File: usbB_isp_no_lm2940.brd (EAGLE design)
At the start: 56 x 20 mm, 9 parts, among them IC2 TINY13-20PU, X1 PN61729-S

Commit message: minor adjustments (tm)
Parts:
- moved C3 0.23 mm to (44.4, 5.65)
- moved IC2 0.23 mm to (37.2, 6.20)
- moved LED1 0.23 mm to (14.6, 9.03)
- moved R1 0.23 mm to (38.7, 13.5)
- moved R2 0.23 mm to (26.2, 12.0)
- moved R3 0.23 mm to (26.5, 5.84)
- moved SV2 0.23 mm to (49.3, 9.03)
- moved X1 0.09 mm to (2.47, 8.94)
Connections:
- net GND: now also X1.2
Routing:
- net GND: track 17.1 -> 25.0 mm

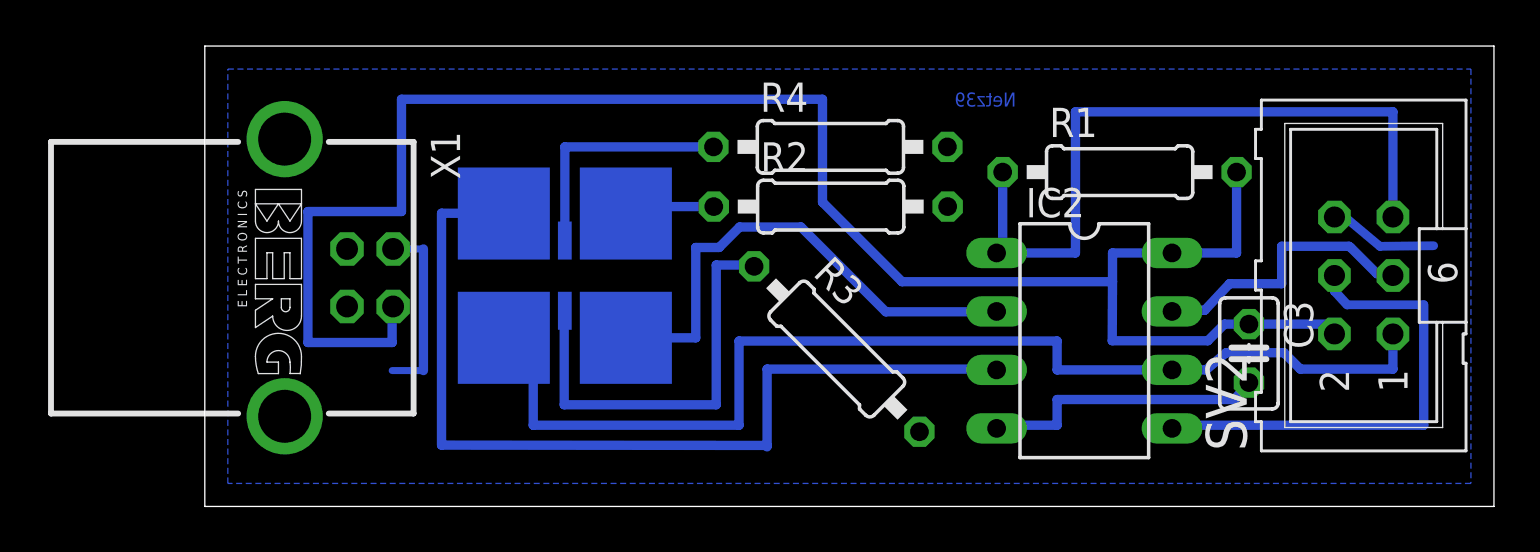
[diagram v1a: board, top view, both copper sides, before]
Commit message: wrong usb-pin *again and again and again and again …
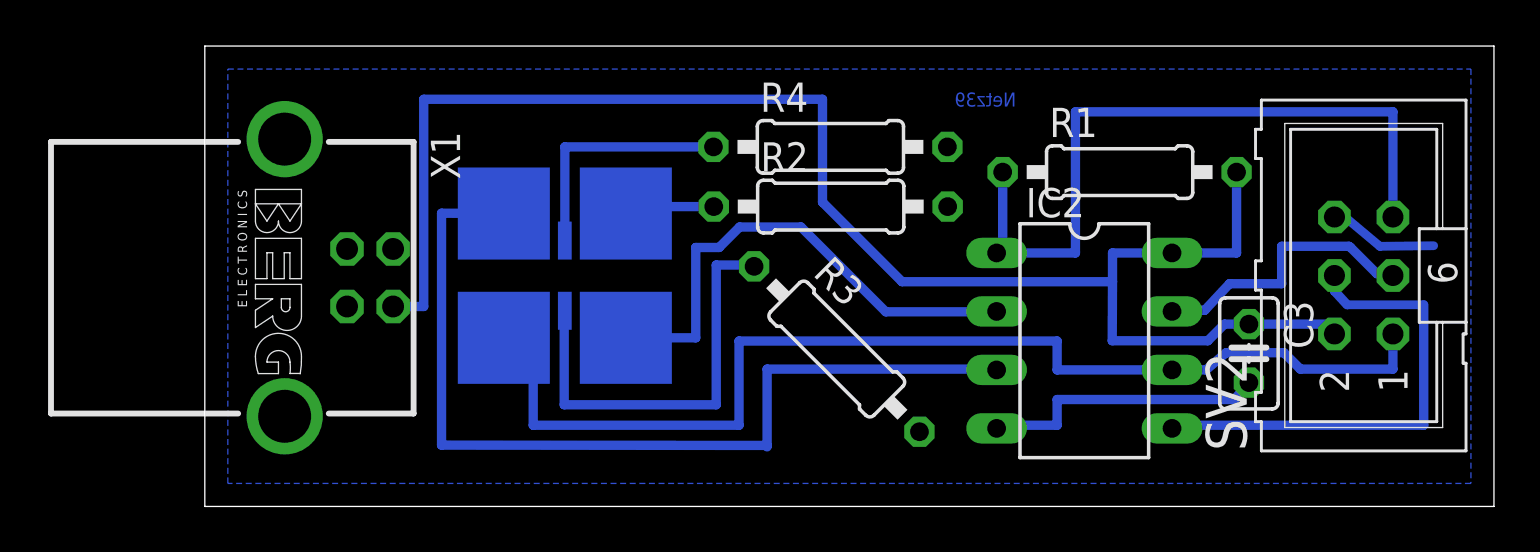
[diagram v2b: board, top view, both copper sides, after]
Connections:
- net GND: now also X1.4; no longer X1.2
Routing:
- net VCC: track 79.8 -> 69.3 mm
- net GND: track 25.0 -> 17.1 mm
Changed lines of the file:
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@@
 <setting verticaltext="up"/>
 </settings>
-<grid distance="39.3700787" unitdist="mil" unit="mil" style="dots" multiple="1" display="yes" altdistance="0.0254" altunitdist="mm" altunit="mm"/>
+<grid distance="1" unitdist="mil" unit="mil" style="dots" multiple="1" display="yes" altdistance="0.0254" altunitdist="mm" altunit="mm"/>
 <layers>
 <layer number="1" name="Top" color="4" fill="1" visible="yes" active="yes"/>
@@
 <wire x1="36.0238" y1="3.6454" x2="43.7228" y2="3.6454" width="0.4064" layer="16"/>
 <wire x1="43.7228" y1="3.6454" x2="44.356" y2="4.3802" width="0.4064" layer="16"/>
-<contactref element="X1" pad="2"/>
-<wire x1="7.1789" y1="10.186" x2="8.4963" y2="10.186" width="0.3048" layer="16"/>
-<wire x1="8.4963" y1="10.186" x2="8.4963" y2="4.9022" width="0.4064" layer="16"/>
-<wire x1="8.4963" y1="4.9022" x2="7.1374" y2="4.9022" width="0.3048" layer="16"/>
 <polygon width="0.4064" layer="16" isolate="0.5842" thermals="no">
 <vertex x="0" y="0"/>
@@
 <vertex x="54" y="0"/>
 </polygon>
+<contactref element="X1" pad="4"/>
 </signal>
 <signal name="VCC">
@@
 <wire x1="44.356" y1="6.9202" x2="48.0716" y2="6.9202" width="0.4064" layer="16"/>
 <wire x1="48.0716" y1="6.9202" x2="48.0716" y2="6.493" width="0.4064" layer="16"/>
-<wire x1="7.1789" y1="7.686" x2="7.1374" y2="7.686" width="0.4064" layer="16"/>
-<wire x1="7.1374" y1="7.686" x2="7.1374" y2="6.1214" width="0.4064" layer="16"/>
-<wire x1="7.1374" y1="6.1214" x2="3.4798" y2="6.1214" width="0.4064" layer="16"/>
-<wire x1="3.4798" y1="6.1214" x2="3.4798" y2="11.811" width="0.4064" layer="16"/>
-<wire x1="3.4798" y1="11.811" x2="7.5438" y2="11.811" width="0.4064" layer="16"/>
-<wire x1="7.5438" y1="11.811" x2="7.5438" y2="16.6878" width="0.4064" layer="16"/>
-<wire x1="7.5438" y1="16.6878" x2="25.8318" y2="16.6878" width="0.4064" layer="16"/>
 <wire x1="41.0156" y1="10.0114" x2="38.4302" y2="10.0114" width="0.4064" layer="16"/>
 <wire x1="38.4302" y1="10.0114" x2="38.4302" y2="8.763" width="0.4064" layer="16"/>
@@
 <wire x1="38.4175" y1="6.1976" x2="38.4302" y2="8.763" width="0.4064" layer="16"/>
 <wire x1="42.5704" y1="6.1976" x2="43.293" y2="6.9202" width="0.4064" layer="16"/>
+<wire x1="7.1374" y1="7.686" x2="8.509" y2="7.686" width="0.4064" layer="16"/>
+<wire x1="8.509" y1="7.686" x2="8.509" y2="16.6878" width="0.4064" layer="16"/>
+<wire x1="8.509" y1="16.6878" x2="25.8318" y2="16.6878" width="0.4064" layer="16"/>
+<wire x1="7.1374" y1="7.686" x2="7.1789" y2="7.686" width="0" layer="19" extent="16-16"/>
 </signal>
 <signal name="_RESET">
